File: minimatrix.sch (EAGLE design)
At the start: 8 parts

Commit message: Rearrange pins so the IR receiver is on an interrupt.
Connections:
- removed net N$21: U$1.PA1(XTAL2), U$2.OUT
- removed net R5: RN1E.1, U$1.(INT0)PD2
- new net N$1: U$1.(INT0)PD2, U$2.OUT
- new net N$3: RN1E.1, U$1.PA1(XTAL2)
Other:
- moved on the sheet: U$2
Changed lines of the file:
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@@
 <instance part="U$1" gate="G$1" x="-2.54" y="66.04"/>
 <instance part="BAT1" gate="G$1" x="-43.18" y="40.64" rot="R270"/>
-<instance part="U$2" gate="G$1" x="-60.96" y="66.04" rot="MR180"/>
+<instance part="U$2" gate="G$1" x="-66.04" y="66.04" rot="MR180"/>
 <instance part="U$3" gate="G$1" x="10.16" y="88.9" rot="MR0"/>
 <instance part="P+1" gate="VCC" x="-43.18" y="48.26"/>
@@
 <instance part="RN1" gate="G" x="45.72" y="22.86"/>
 <instance part="RN1" gate="H" x="45.72" y="17.78"/>
-<instance part="P+3" gate="VCC" x="-50.8" y="73.66"/>
-<instance part="GND3" gate="1" x="-50.8" y="63.5"/>
+<instance part="P+3" gate="VCC" x="-55.88" y="73.66"/>
+<instance part="GND3" gate="1" x="-55.88" y="63.5"/>
 <instance part="C1" gate="G$1" x="-33.02" y="40.64"/>
 <instance part="C2" gate="G$1" x="-27.94" y="40.64"/>
@@
 </segment>
 </net>
-<net name="R5" class="0">
-<segment>
-<pinref part="U$1" gate="G$1" pin="(INT0)PD2"/>
-<wire x1="15.24" y1="43.18" x2="33.02" y2="43.18" width="0.1524" layer="91"/>
-<wire x1="33.02" y1="43.18" x2="33.02" y2="33.02" width="0.1524" layer="91"/>
-<pinref part="RN1" gate="E" pin="1"/>
-<wire x1="33.02" y1="33.02" x2="40.64" y2="33.02" width="0.1524" layer="91"/>
-</segment>
-</net>
 <net name="R6" class="0">
 <segment>
@@
 <pinref part="U$1" gate="G$1" pin="PA0(XTAL1)"/>
 <wire x1="-53.34" y1="55.88" x2="-22.86" y2="55.88" width="0.1524" layer="91"/>
-</segment>
-</net>
-<net name="N$21" class="0">
-<segment>
-<pinref part="U$2" gate="G$1" pin="OUT"/>
-<pinref part="U$1" gate="G$1" pin="PA1(XTAL2)"/>
-<wire x1="-50.8" y1="60.96" x2="-22.86" y2="60.96" width="0.1524" layer="91"/>
 </segment>
 </net>
@@
 </segment>
 </net>
+<net name="N$1" class="0">
+<segment>
+<pinref part="U$2" gate="G$1" pin="OUT"/>
+<wire x1="-55.88" y1="60.96" x2="-50.8" y2="60.96" width="0.1524" layer="91"/>
+<wire x1="-50.8" y1="60.96" x2="-50.8" y2="27.94" width="0.1524" layer="91"/>
+<wire x1="-50.8" y1="27.94" x2="17.78" y2="27.94" width="0.1524" layer="91"/>
+<wire x1="17.78" y1="27.94" x2="17.78" y2="43.18" width="0.1524" layer="91"/>
+<pinref part="U$1" gate="G$1" pin="(INT0)PD2"/>
+<wire x1="17.78" y1="43.18" x2="15.24" y2="43.18" width="0.1524" layer="91"/>
+</segment>
+</net>
+<net name="N$3" class="0">
+<segment>
+<pinref part="RN1" gate="E" pin="1"/>
+<wire x1="40.64" y1="33.02" x2="20.32" y2="33.02" width="0.1524" layer="91"/>
+<wire x1="20.32" y1="33.02" x2="20.32" y2="25.4" width="0.1524" layer="91"/>
+<wire x1="20.32" y1="25.4" x2="-48.26" y2="25.4" width="0.1524" layer="91"/>
+<wire x1="-48.26" y1="25.4" x2="-48.26" y2="60.96" width="0.1524" layer="91"/>
+<pinref part="U$1" gate="G$1" pin="PA1(XTAL2)"/>
+<wire x1="-48.26" y1="60.96" x2="-22.86" y2="60.96" width="0.1524" layer="91"/>
+</segment>
+</net>

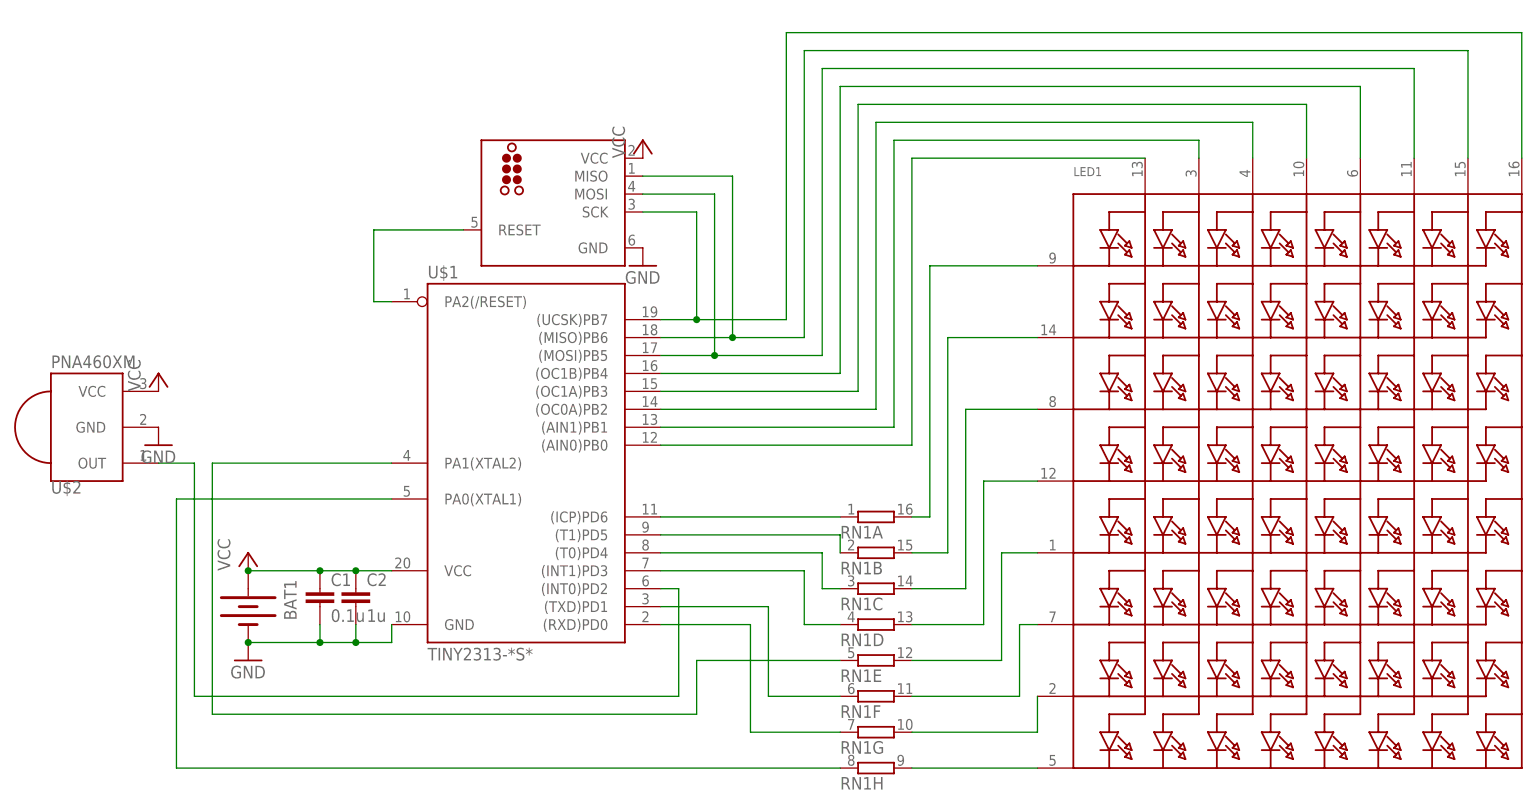
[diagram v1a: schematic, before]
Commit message: Rewire with fixed pinouts and better connection for IR receiver.
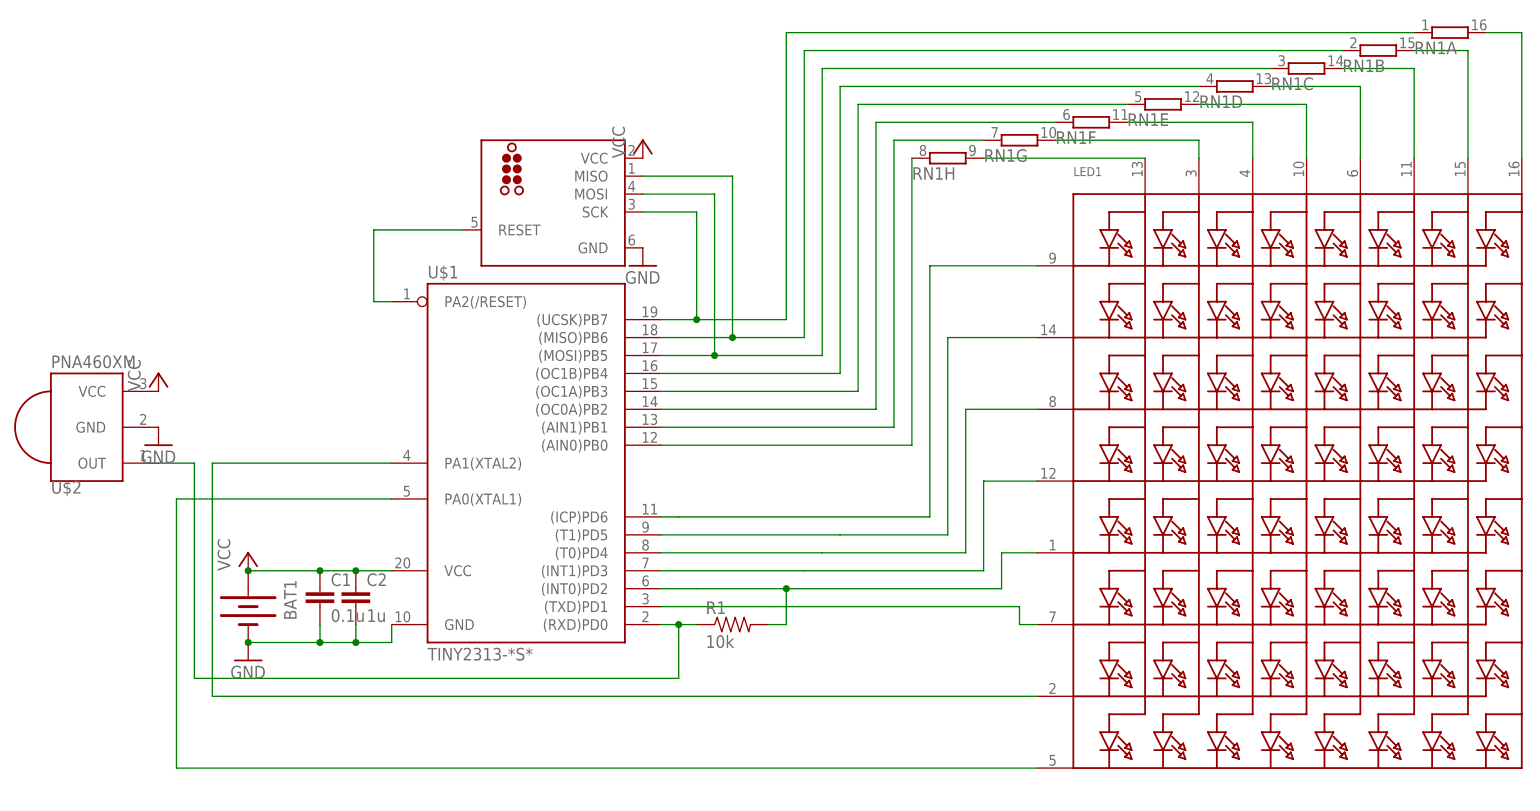
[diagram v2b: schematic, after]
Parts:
- added R1: 10k, SparkFun-Passives:RESISTOR0805-RES
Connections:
- removed net R1: RN1A.1, U$1.(ICP)PD6
- removed net ROW2: LED1.K2, RN1B.2
- removed net ROW3: LED1.K3, RN1C.2
- removed net ROW4: LED1.K4, RN1D.2
- removed net ROW6: LED1.K6, RN1F.2
- removed net ROW7: LED1.K7, RN1G.2
- removed net ROW8: LED1.K8, RN1H.2
- new net N$10: LED1.A1, RN1H.2
- new net N$11: LED1.K5, R1.2, U$1.(INT0)PD2
- new net N$4: LED1.A3, RN1F.2
- new net N$5: LED1.A4, RN1E.2
- new net N$6: LED1.A5, RN1D.2
- new net N$7: LED1.A6, RN1C.2
- new net N$8: LED1.A7, RN1B.2
- new net N$9: LED1.A8, RN1A.2
- net C1: now also RN1H.1; no longer LED1.A1
- net C2: now also RN1G.1; no longer LED1.A2
- net C3: now also RN1F.1; no longer LED1.A3
- net C4: now also RN1E.1; no longer LED1.A4
- net C5: now also RN1D.1; no longer LED1.A5
- net C6: now also RN1C.1; no longer LED1.A6
- net C7: now also RN1B.1; no longer LED1.A7
- net C8: now also RN1A.1; no longer LED1.A8
- net N$1: now also R1.1, U$1.(RXD)PD0; no longer U$1.(INT0)PD2
- net N$3: now also LED1.A2, RN1G.2; no longer RN1E.1, U$1.PA1(XTAL2)
- net R2: now also LED1.K2; no longer RN1B.1
- net R3: now also LED1.K3; no longer RN1C.1
- net R4: now also LED1.K4; no longer RN1D.1
- net R6: now also LED1.K6; no longer RN1F.1
- net R7: now also LED1.K7; no longer RN1G.1, U$1.(RXD)PD0
- net R8: now also LED1.K8; no longer RN1H.1
- net ROW1: now also U$1.(ICP)PD6; no longer RN1A.2
- net ROW5: now also U$1.PA1(XTAL2); no longer LED1.K5, RN1E.2
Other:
- moved on the sheet: RN1A, RN1B, RN1C, RN1D, RN1E, RN1F, RN1G, RN1H
